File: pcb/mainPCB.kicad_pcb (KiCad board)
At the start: 4 copper layers, 160 x 73.2 mm, 162 parts, among them IC1 FXL6408UMX, IC2 ATA6561-GAQW-N, IC3 ICL3221EIVZ, J1 PTSM-Header-Horizontal-6, J10 Conn_01x08_Female, J11 Conn_01x08_Female, J12 Conn_02x02_Odd_Even, J13 SM04B-SRSS-TB(LF)(SN), J14 USB_B_Micro, J15 RJ45_Amphenol_RJMG1BD3B8K1ANR, J16 DB9_Male_MountingHoles, J17 SM04B-SRSS-TB(LF)(SN), J18 PTSM-Header-Horizontal-2, J3 PTSM-Header-Horizontal-7, J4 CCA-Header-Horizontal-4, J5 PTSM-Header-Horizontal-5, J7 Conn_01x04_Male, J8 Conn_01x04_Male, J9 Conn_01x08_Female, K1 CP1SA-12V-Z, K2 CP1SA-12V-Z, Q1 BC817-40,215, Q2 BC817-40,215, SW1 SW_Push, U1 ESP32-WROOM-32, U10 NUD3124LT1G, U11 LAN8720A, U12 LSM9DS1, U2 AZ1117-3.3, U3 VNH7070AS, U4 ADS1115IDGS, U5 VNH7070AS, U6 PCA9306DCTR, U7 TPD3E001DRLR, U8 CP2102N-A01-GQFN24, U9 VNH7070AS

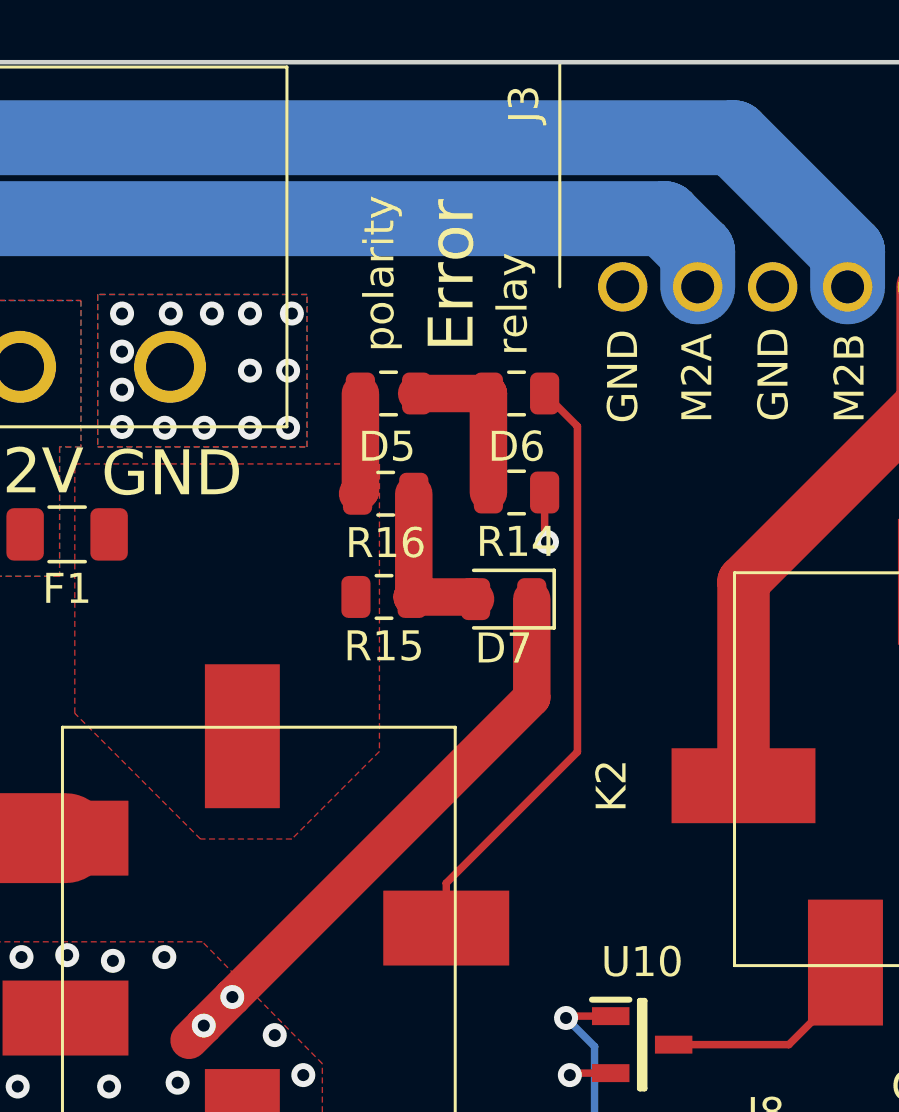
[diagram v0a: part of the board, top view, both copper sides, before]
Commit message: removed the relais-error led
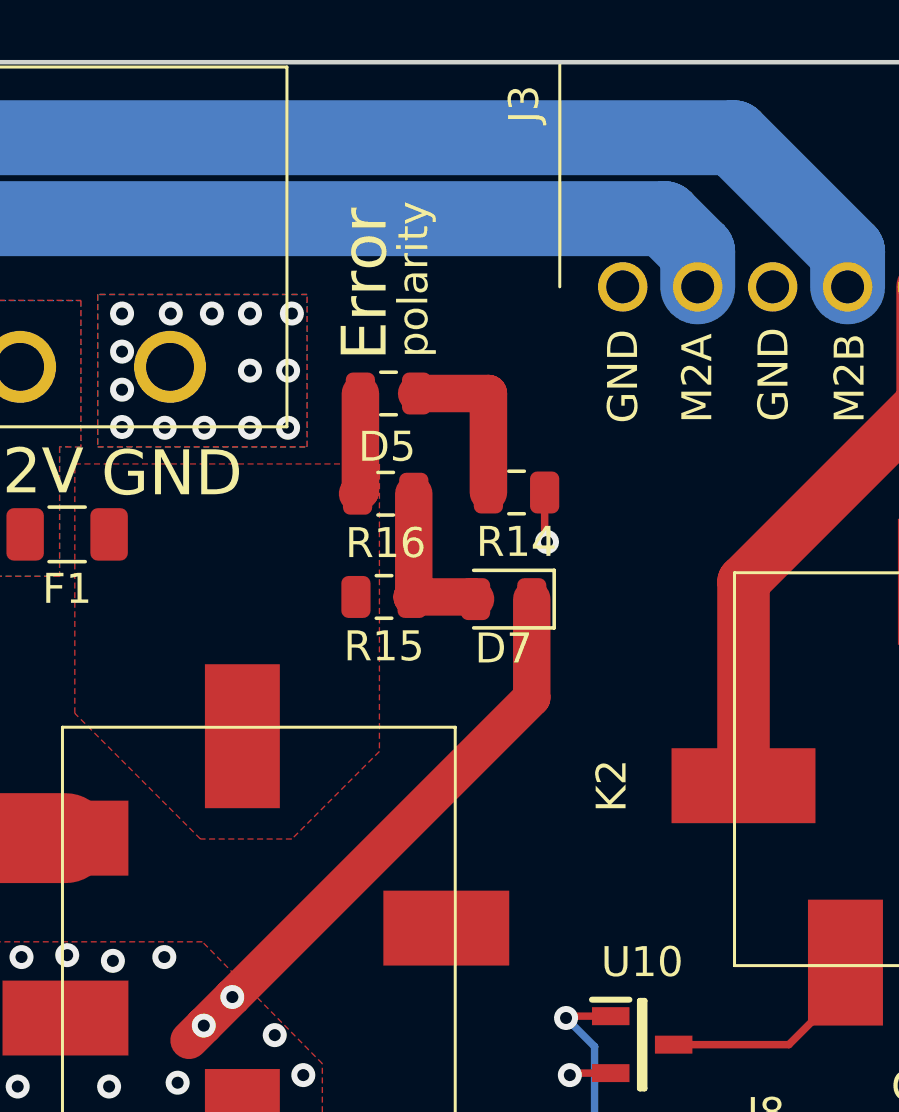
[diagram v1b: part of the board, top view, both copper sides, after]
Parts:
- removed D6: LED/red, Capacitor_SMD:C_0805_2012Metric
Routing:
- net Net-(K1-Pad5): track 20.1 -> 0.00 mm
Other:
- board text removed: "relay"

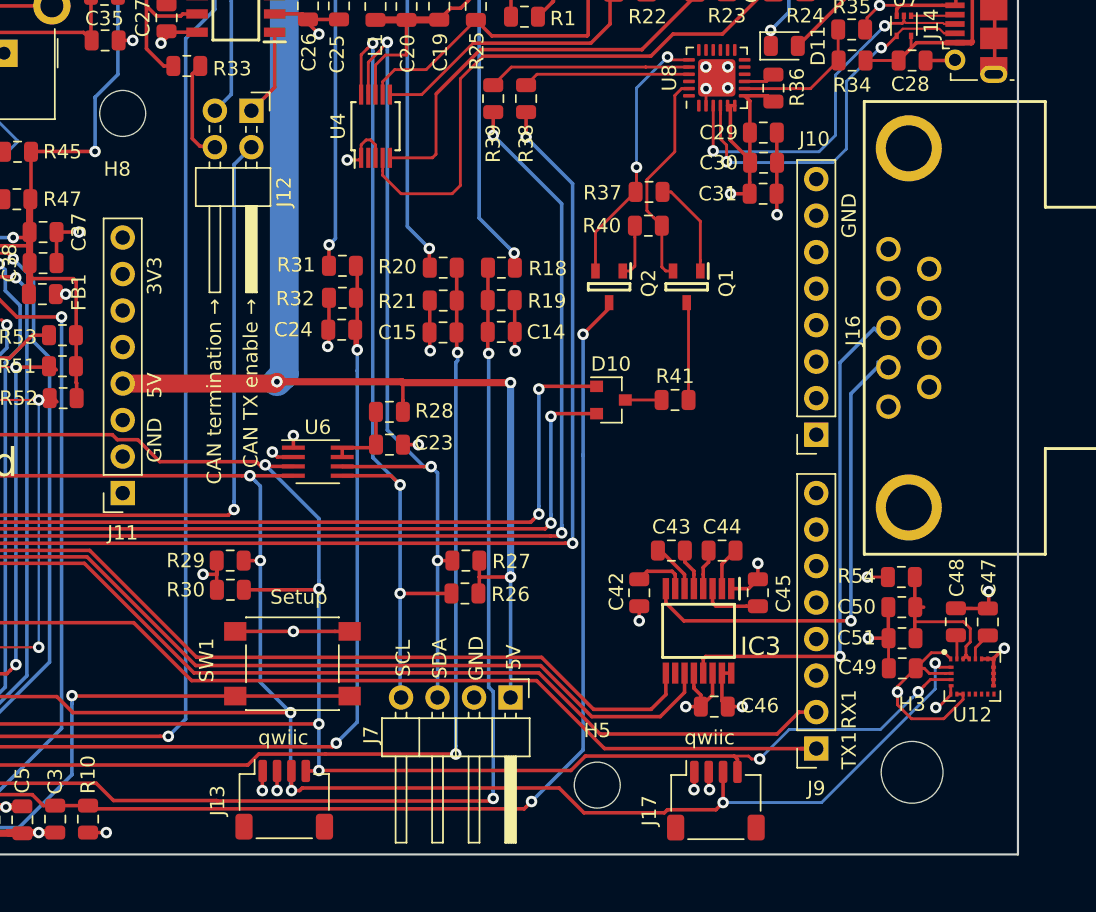
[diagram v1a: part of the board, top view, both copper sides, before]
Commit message: Moved the LSM9DS1 under F9P board, fixes #6
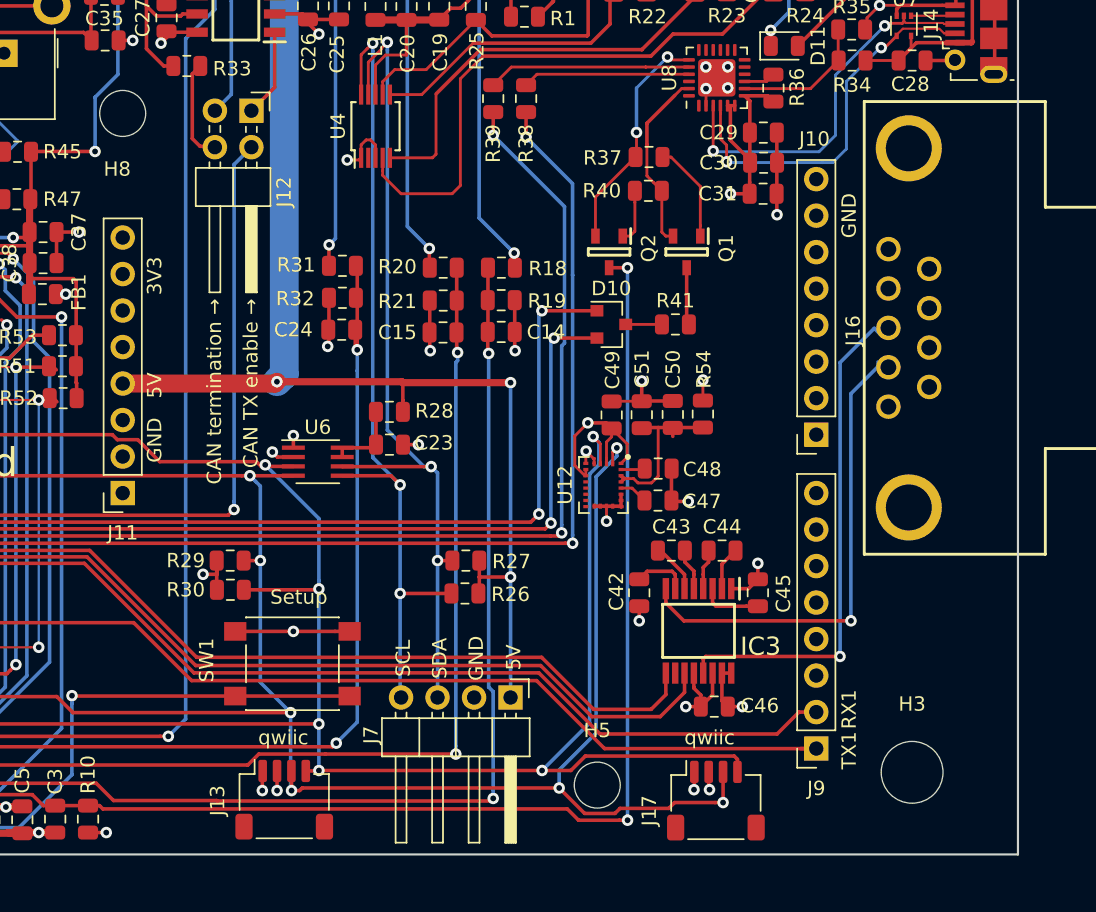
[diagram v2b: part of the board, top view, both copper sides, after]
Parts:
- moved U12 28.9 mm to (148.6, 84.9), turned to 270 degrees
- moved C49 26.8 mm to (149.2, 80.0), turned to 270 degrees
- moved C47 24.5 mm to (152.4, 86.0), turned to 180 degrees
- moved C51 23.9 mm to (151.3, 80.0), turned to 270 degrees
- moved C48 23.3 mm to (152.4, 83.8), turned to 180 degrees
- moved C50 20.8 mm to (153.5, 80.0), turned to 270 degrees
- moved R54 17.9 mm to (155.6, 80.0), turned to 270 degrees
- moved D10 5.26 mm to (149.2, 73.7)
- moved R41 5.26 mm to (153.6, 73.7)
- moved Q1 2.43 mm to (154.4, 68.7)
- moved Q2 2.43 mm to (149.0, 68.7)
- moved R37 2.43 mm to (151.8, 62.1)
- moved R40 2.43 mm to (151.8, 64.4)
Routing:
- net /ESP_EN: track 78.3 -> 88.2 mm
- net /I2C_3_SDA: track 177.0 -> 186.7 mm
- net /I2C_3_SCL: track 180.1 -> 185.6 mm, vias 8 -> 9
- net /M1_INB: track 103.7 -> 108.9 mm
- net /M1_INA: track 108.7 -> 114.0 mm
- net +3V3: track 86.8 -> 84.0 mm
- net Net-(Q1-Pad3): track 6.83 -> 4.19 mm
- net Net-(Q2-Pad2): track 18.5 -> 16.1 mm
- net Net-(Q1-Pad2): track 15.3 -> 12.8 mm

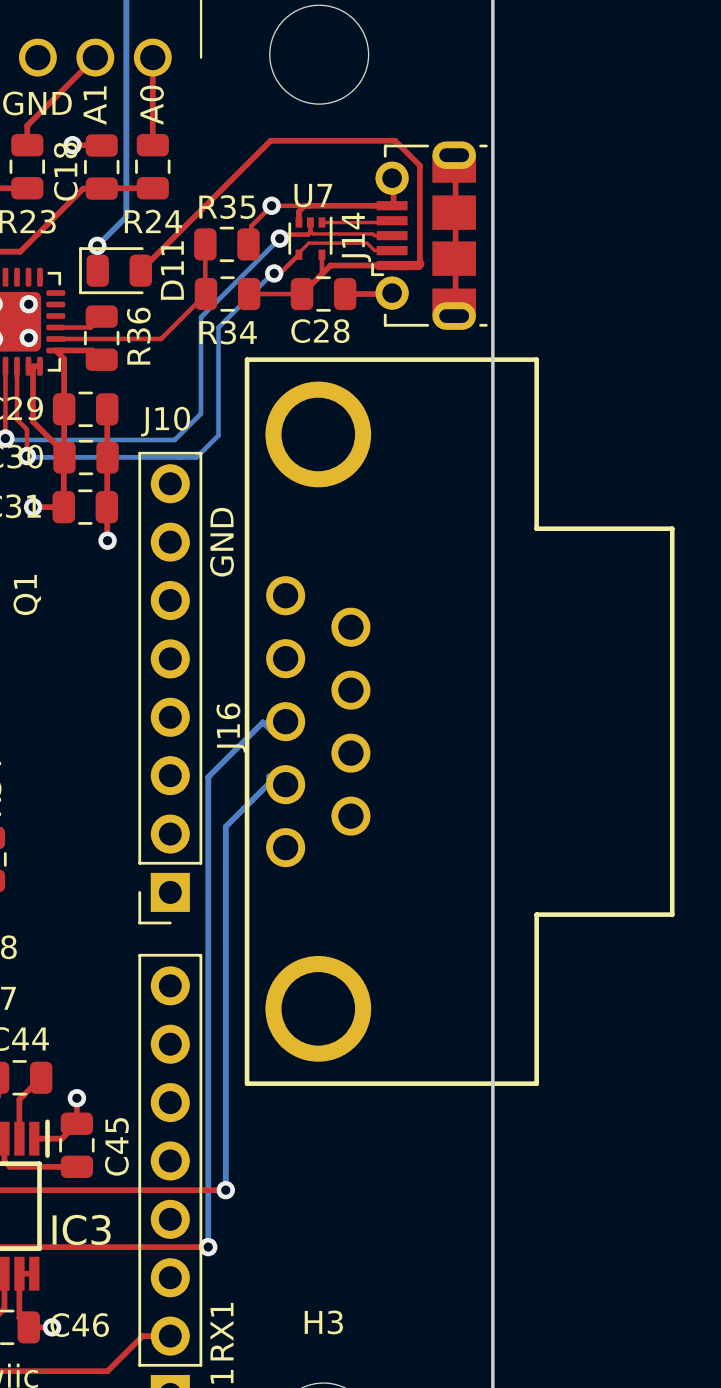
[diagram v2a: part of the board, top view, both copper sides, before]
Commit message: Moved the USB and RS232 connectors a bit, more distance, so easier to use both at the same time
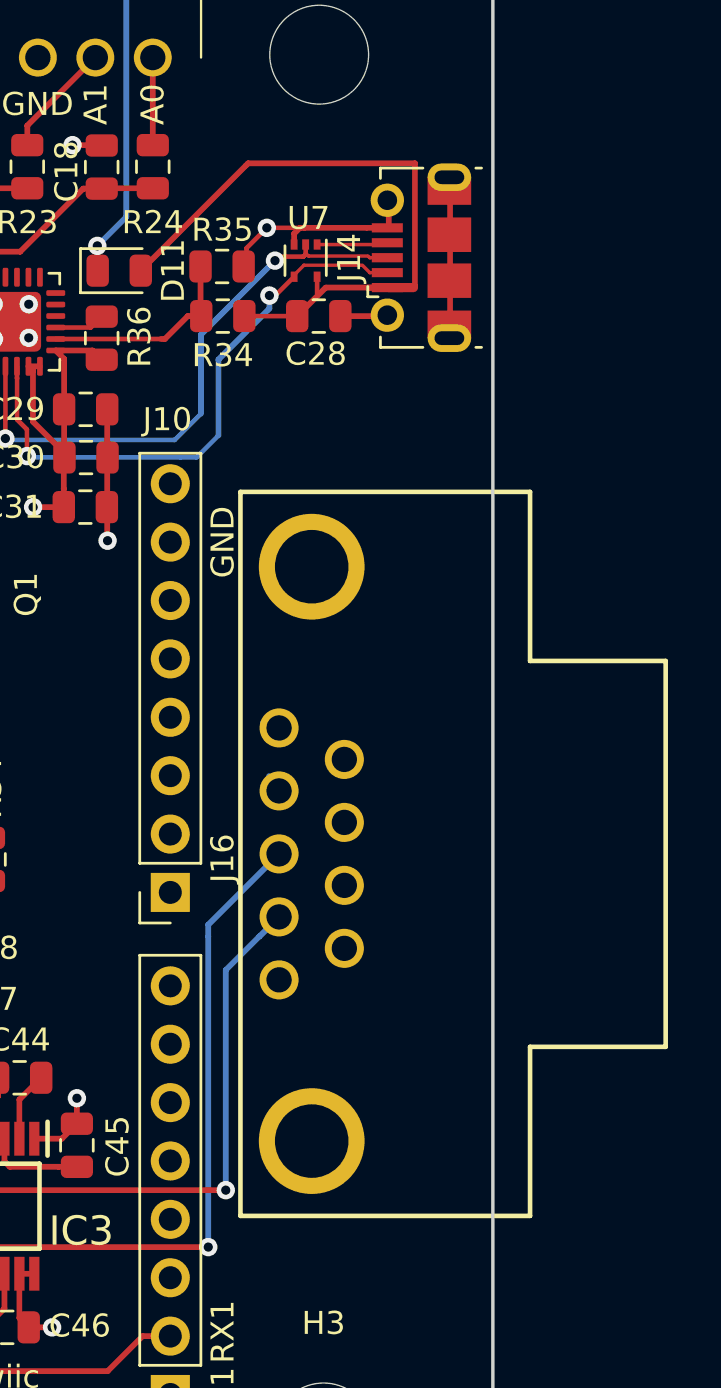
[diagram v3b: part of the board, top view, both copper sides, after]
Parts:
- moved J16 5.76 mm to (179.1, 79.7)
- moved C28 0.98 mm to (169.9, 56.3)
- moved R34 0.98 mm to (165.7, 56.3)
- moved J14 0.98 mm to (174.4, 53.8)
- moved R35 0.98 mm to (165.7, 54.2)
- moved U7 0.98 mm to (169.3, 53.9)
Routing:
- net Net-(IC3-Pad13): track 34.9 -> 29.0 mm
- net Net-(IC3-Pad8): track 33.2 -> 27.2 mm
- net Net-(J14-Pad3): track 27.1 -> 26.0 mm
- net Net-(J14-Pad2): track 26.8 -> 25.8 mm
- net Net-(R34-Pad1): track 9.52 -> 8.91 mm
- net GND: track 283.1 -> 283.6 mm

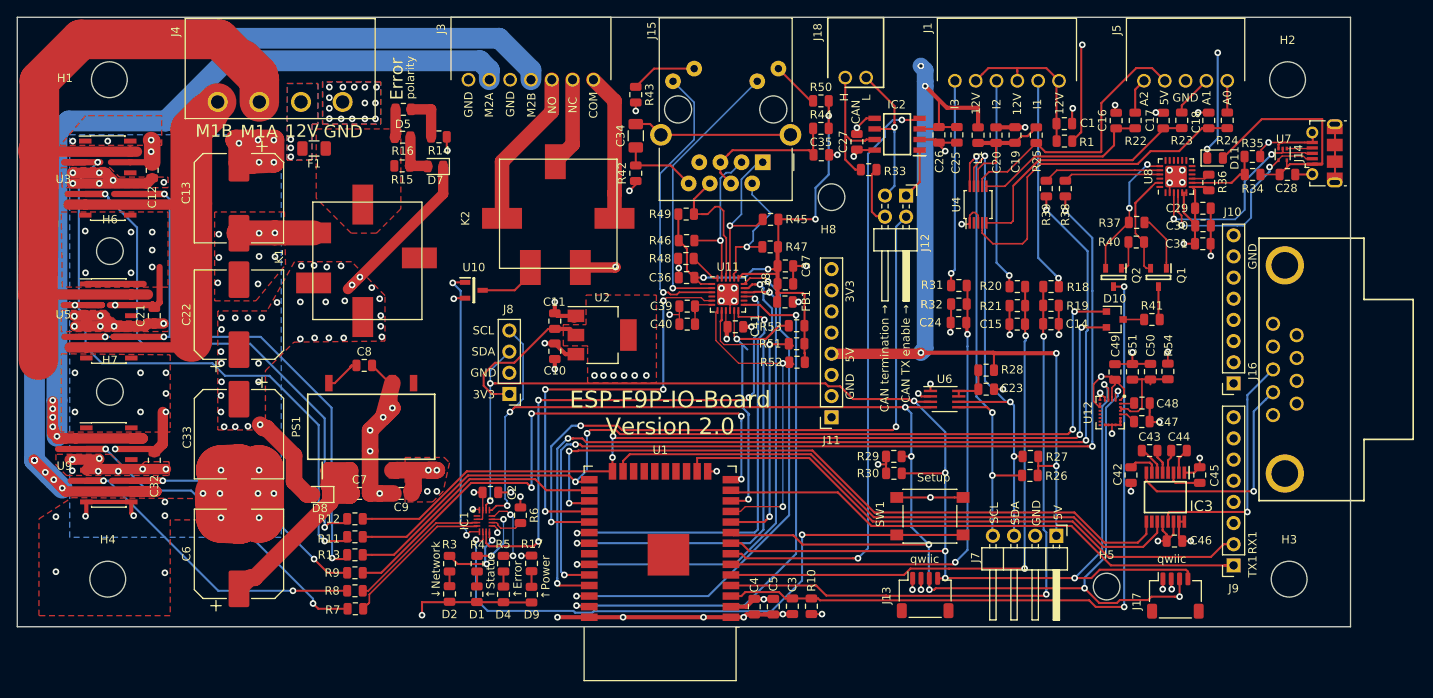
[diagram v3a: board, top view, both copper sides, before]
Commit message: Reduced the number of vias
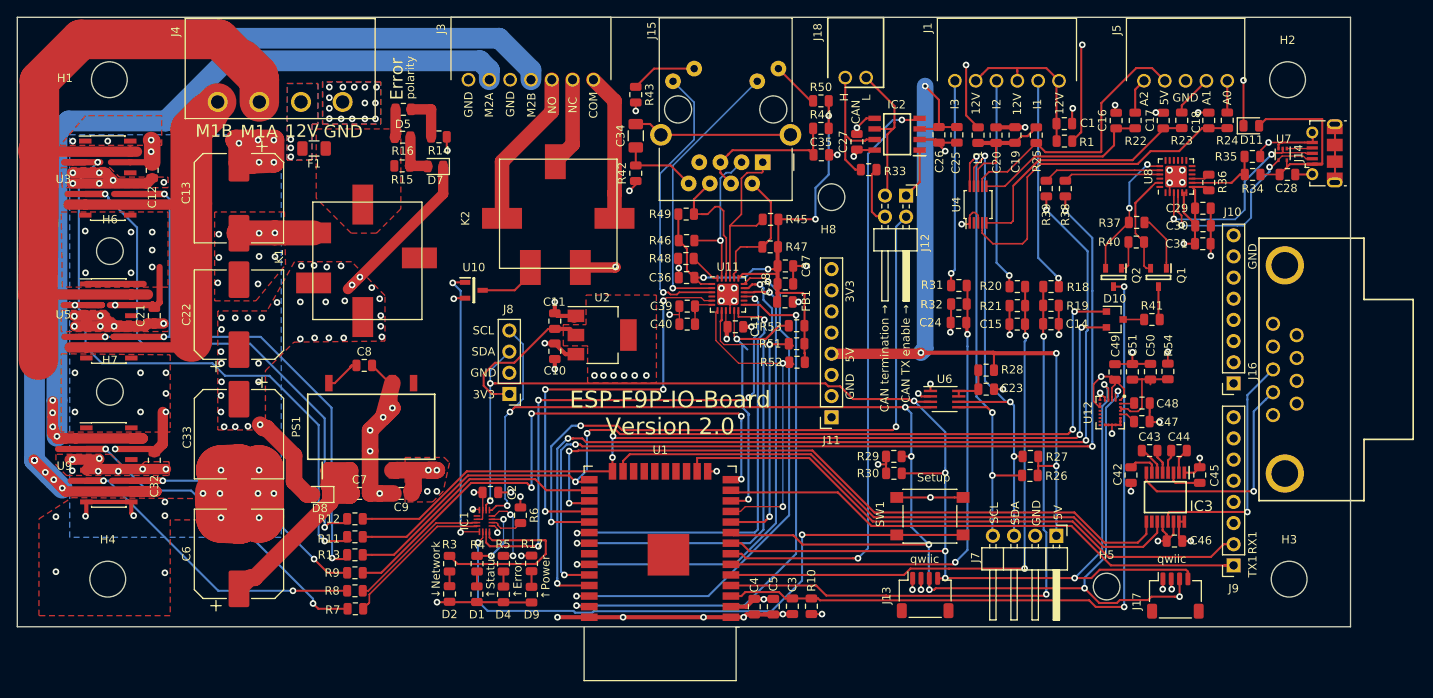
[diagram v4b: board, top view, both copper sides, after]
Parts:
- moved D11 5.82 mm to (165.6, 50.5)
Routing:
- net Net-(IC1-Pad8): track 9.29 -> 21.6 mm, vias 2 -> 0
- net +5V: track 137.5 -> 125.9 mm, vias 12 -> 11
- net Net-(C28-Pad1): track 30.4 -> 24.5 mm
- net GND: track 283.6 -> 280.2 mm
- net Net-(J15-PadR1): track 20.1 -> 21.4 mm, vias 1 -> 0
- net /LAN8720/TD-: track 16.8 -> 15.7 mm, vias 1 -> 0
- net Net-(IC1-Pad6): track 75.3 -> 74.5 mm
- net Net-(IC2-Pad6): track 18.4 -> 18.2 mm, vias 1 -> 0
- net /sheet5C9DA53F/outA: vias 5 -> 4
